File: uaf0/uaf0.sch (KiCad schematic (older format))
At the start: 6 parts, among them X1 Клеммник_х2, X2 Клеммник_х2, X3 Клеммник_х2, X4 Клеммник_х2, X5 Клеммник_х2

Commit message: схема+трассировка, требуется проверка
не установлена ссылка на инстаграм
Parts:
- added C1, C2, C3, C4, C5, C6, C7, C8: Конденсатор_керамический, N_RLC:Конденсатор_SMD_0603, symbol elements:Конденсатор_керамический
- added DD2: 5559ИН10_28(UART-RS485), N_DD:SO-8, symbol elements:5559ИН10_28(UART-RS485)
- added FU1: Предохранитель_0.1A, N_RLC:Предохранитель_SMD_1812, symbol elements:Предохранитель
- added G1: стабилизатор_нерегулируемый_LM1117GS-5.0, N_VD_HL:Транзистор_NPN_SOT223, symbol elements:стабилизатор_нерегулируемый_LM1117GS-5.0
- added G2: стабилизатор_нерегулируемый_XC6206P302MR, N_VD_HL:Транзистор_IRLML6344TR_SOT-23, symbol elements:стабилизатор_нерегулируемый_XC6206P302MR
- added HL1, HL2: Светодиод, N_VD_HL:Светодиод_SMD_0603, symbol elements:Светодиод
- added R1, R10, R11, R2, R3, R4, R5, R6, R7, R8, R9: Резистор_0,065Вт, N_RLC:Резистор_SMD_0603_0,065_Вт, symbol elements:Резистор_0,065Вт
- added VD1: Диод_шоттки_S13, N_VD_HL:Диод_S13_SOD-123, symbol elements:Диод_шоттки
- added X6, X7, X8: Клеммник_х2, N_X:Клеммник_х2_шаг5, symbol elements:Клеммник_х2
- added XP1: Вилка_PLD6_ПРОГ, N_X:Вилка_PLD6_вертикальная, symbol elements:Вилка_PLD6_ПРОГ
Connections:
- net 12V: now also C4.1, G1.3 (6...30_В)
- net GND: now also DD1.21 (GND), DD1.3 (GND), DD1.5 (GND), C1.2, C2.2, C3.1, C4.2, C5.2, C6.2, C7.2, C8.2, DD2.5 (GND), FU1.2, G1.1 (GND), G2.1 (GND), HL1.2, HL2.2, R7.2, X8.1, X8.2, XP1.6 (GND); no longer X2.1, X2.2
- net PD3_INT1: now reaches DD1.1 (PD3(INT1))
- net PB0: now reaches DD1.12 (PB0(ICP1))
- net PB0: now also DD2.2 (nRE), DD2.3 (DE), R7.1
- net PB1_OC1A: now reaches DD1.13 (PB1(OC1A))
- net PB2_OC1B: now reaches DD1.14 (PB2(SS/OC1B))
- net MOSI: now reaches DD1.15 (PB3(MOSI/OC2))
- net MOSI: now also R11.2
- net MISO: now reaches DD1.16 (PB4(MISO))
- net MISO: now also R8.1
- net SCK: now reaches DD1.17 (PB5(SCK))
- net SCK: now also R9.1
- net 5V: now reaches DD1.18 (AVCC)
- net 5V: now also DD1.4 (VCC), DD1.6 (VCC), C1.1, C2.1, C3.2, C5.1, C6.1, DD2.8 (Ucc), G1.2 (5В), G2.3 (3,2...6_В), R1.1, R10.1, R2.1, R4.1, VD1.2
- net 3V: now reaches DD1.20 (AREF)
- net 3V: now also C7.1, C8.1, G2.2 (3В)
- net PC0: now reaches DD1.23 (PCO(ADC0))
- net PC1: now reaches DD1.24 (PC1(ADC1))
- net PC3: now reaches DD1.26 (PC3(ADC3))
- net PC3: now also R5.1
- net SDA: now reaches DD1.27 (PC4(ADC4/SDA))
- net SDA: now also R1.2, X6.1
- net SCL: now reaches DD1.28 (PC5(ADC5/SCL))
- net SCL: now also R2.2, X6.2
- net RES: now reaches DD1.29 (PC6(RESET))
- net RES: now also R10.2, XP1.5 (RST)
- net RX: now reaches DD1.30 (PD0(RXD))
- net RX: now also R3.2
- net TX: now reaches DD1.31 (PD1(TXD))
- net TX: now also R6.2
- net PD2_INT0: now reaches DD1.32 (PD2(INT0))
- new net: DD2.1 (RO), R3.1
- new net: DD2.4 (DI), R6.1
- new net: R8.2, XP1.1 (MISO)
- new net: R9.2, XP1.3 (SCK)
- new net: R11.1, XP1.4 (MOSI)
- new net: HL2.1, R5.2
- new net: HL1.1, R4.2
- new net PWR_GND: FU1.1, X2.1, X2.2
- new net RS485_A: DD2.6 (AY), X7.1
- new net RS485_B: DD2.7 (BZ), X7.2
- new net VCC_PROG: VD1.1, XP1.2 (VCC)
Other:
- moved on the sheet: DD1, X1, X2, X3, X4, X5

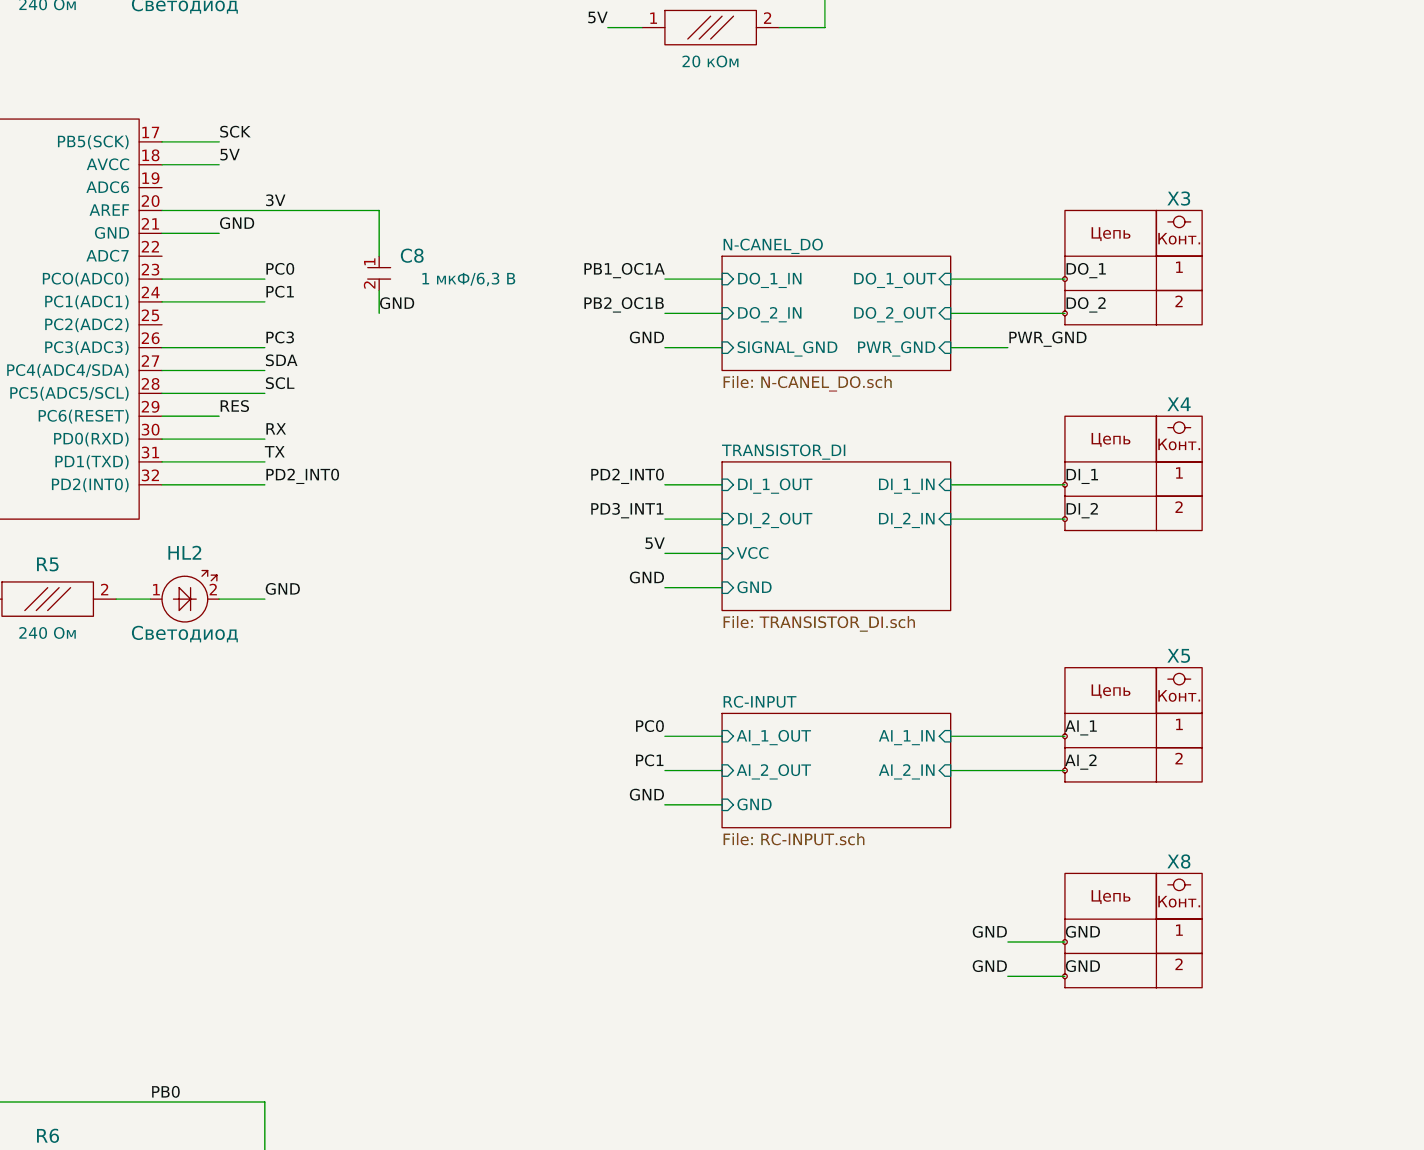
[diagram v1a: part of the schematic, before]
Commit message: исправлена шелкография, добавлены файлы производства v0
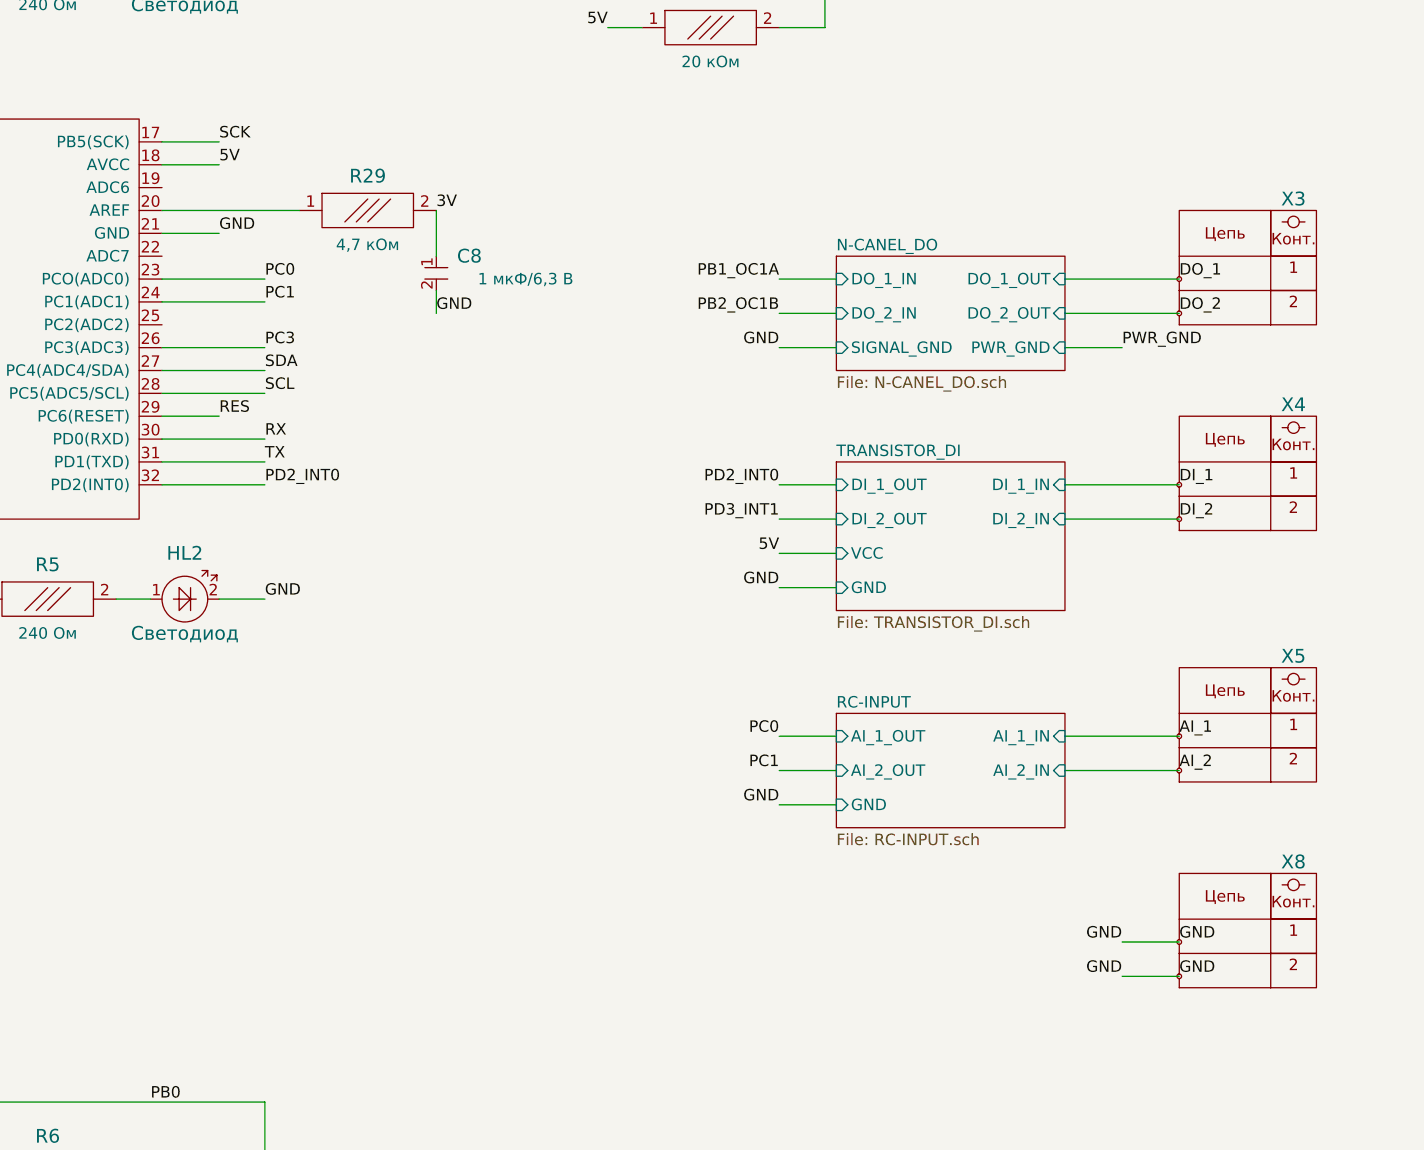
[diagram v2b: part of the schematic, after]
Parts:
- added R29: Резистор_0,065Вт, N_RLC:Резистор_SMD_0603_0,065_Вт, symbol elements:Резистор_0,065Вт
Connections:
- net 3V: now also R29.2; no longer DD1.20 (AREF)
- new net: DD1.20 (AREF), R29.1
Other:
- moved on the sheet: C8, X3, X4, X5, X8
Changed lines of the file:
@@
 L elements:Клеммник_х2 X3
 U 1 1 5DAC06C7
-P 9500 3100
-F 0 "X3" H 9000 3450 60  0000 C CNN
-F 1 "Клеммник_х2" H 9450 2725 60  0001 C CNN
-F 2 "N_X:Клеммник_х2_шаг5" H 9500 3100 60  0001 C CNN
-F 3 "" H 9500 3100 60  0001 C CNN
-	1    9500 3100
+P 10000 3100
+F 0 "X3" H 9500 3450 60  0000 C CNN
+F 1 "Клеммник_х2" H 9950 2725 60  0001 C CNN
+F 2 "N_X:Клеммник_х2_шаг5" H 10000 3100 60  0001 C CNN
+F 3 "" H 10000 3100 60  0001 C CNN
+	1    10000 3100
 	-1   0    0    -1
 $EndComp
-Text Label 9500 3100 0    50   ~ 0
+Text Label 10000 3100 0    50   ~ 0
 DO_1
-Text Label 9500 3250 0    50   ~ 0
+Text Label 10000 3250 0    50   ~ 0
 DO_2
 $Comp
 L elements:Клеммник_х2 X4
 U 1 1 5DAC910B
-P 9500 4000
-F 0 "X4" H 9000 4350 60  0000 C CNN
-F 1 "Клеммник_х2" H 9450 3625 60  0001 C CNN
-F 2 "N_X:Клеммник_х2_шаг5" H 9500 4000 60  0001 C CNN
-F 3 "" H 9500 4000 60  0001 C CNN
-	1    9500 4000
+P 10000 4000
+F 0 "X4" H 9500 4350 60  0000 C CNN
+F 1 "Клеммник_х2" H 9950 3625 60  0001 C CNN
+F 2 "N_X:Клеммник_х2_шаг5" H 10000 4000 60  0001 C CNN
+F 3 "" H 10000 4000 60  0001 C CNN
+	1    10000 4000
 	-1   0    0    -1
 $EndComp
-Text Label 9500 4000 0    50   ~ 0
+Text Label 10000 4000 0    50   ~ 0
 DI_1
-Text Label 9500 4150 0    50   ~ 0
+Text Label 10000 4150 0    50   ~ 0
 DI_2
 $Comp
 L elements:Клеммник_х2 X5
 U 1 1 5DACA5D7
-P 9500 5100
-F 0 "X5" H 9000 5450 60  0000 C CNN
-F 1 "Клеммник_х2" H 9450 4725 60  0001 C CNN
-F 2 "N_X:Клеммник_х2_шаг5" H 9500 5100 60  0001 C CNN
-F 3 "" H 9500 5100 60  0001 C CNN
-	1    9500 5100
+P 10000 5100
+F 0 "X5" H 9500 5450 60  0000 C CNN
+F 1 "Клеммник_х2" H 9950 4725 60  0001 C CNN
+F 2 "N_X:Клеммник_х2_шаг5" H 10000 5100 60  0001 C CNN
+F 3 "" H 10000 5100 60  0001 C CNN
+	1    10000 5100
 	-1   0    0    -1
 $EndComp
-Text Label 9500 5100 0    50   ~ 0
+Text Label 10000 5100 0    50   ~ 0
 AI_1
-Text Label 9500 5250 0    50   ~ 0
+Text Label 10000 5250 0    50   ~ 0
 AI_2
 $Comp
@@
 Text Label 5250 1500 0    50   ~ 0
 GND
-Text Label 6000 2800 0    50   ~ 0
+Text Label 6750 2800 0    50   ~ 0
 3V
 Text Label 5800 2600 0    50   ~ 0
@@
 Text Label 3250 3000 2    50   ~ 0
 5V
-Wire Wire Line
-	5550 2800 6500 2800
 $Comp
 L elements:Конденсатор_керамический C8
 U 1 1 5DAE7890
-P 6500 3050
-F 0 "C8" V 6450 3250 60  0000 R CNN
-F 1 "Конденсатор_керамический" H 6600 2950 60  0001 C CNN
-F 2 "N_RLC:Конденсатор_SMD_0603" H 6500 3050 60  0001 C CNN
-F 3 "" H 6500 3050 60  0001 C CNN
-F 4 "1 мкФ/6,3 В" V 6550 3650 50  0000 R CNN "Номинал"
-F 5 "С111" H 6500 3050 50  0001 C CNN "УГО"
-	1    6500 3050
+P 6750 3050
+F 0 "C8" V 6700 3250 60  0000 R CNN
+F 1 "Конденсатор_керамический" H 6850 2950 60  0001 C CNN
+F 2 "N_RLC:Конденсатор_SMD_0603" H 6750 3050 60  0001 C CNN
+F 3 "" H 6750 3050 60  0001 C CNN
+F 4 "1 мкФ/6,3 В" V 6800 3650 50  0000 R CNN "Номинал"
+F 5 "С111" H 6750 3050 50  0001 C CNN "УГО"
+	1    6750 3050
 	0    1    1    0
 $EndComp
 Wire Wire Line
-	6500 2800 6500 3000
-Wire Wire Line
-	6500 3150 6500 3250
-Text Label 6500 3250 0    50   ~ 0
+	6750 2800 6750 3000
+Wire Wire Line
+	6750 3150 6750 3250
+Text Label 6750 3250 0    50   ~ 0
 GND
 $Comp
@@
 	1000 3000 1750 3000
 $Sheet
-S 8000 3900 1000 650
+S 8500 3900 1000 650
 U 5DB51AF8
 F0 "TRANSISTOR_DI" 50
 F1 "TRANSISTOR_DI.sch" 50
-F2 "DI_1_IN" I R 9000 4000 50
-F3 "GND" I L 8000 4450 50
-F4 "DI_2_IN" I R 9000 4150 50
-F5 "DI_2_OUT" I L 8000 4150 50
-F6 "DI_1_OUT" I L 8000 4000 50
-F7 "VCC" I L 8000 4300 50
+F2 "DI_1_IN" I R 9500 4000 50
+F3 "GND" I L 8500 4450 50
+F4 "DI_2_IN" I R 9500 4150 50
+F5 "DI_2_OUT" I L 8500 4150 50
+F6 "DI_1_OUT" I L 8500 4000 50
+F7 "VCC" I L 8500 4300 50
 $EndSheet
 Wire Wire Line
-	9000 4000 9500 4000
-Wire Wire Line
-	9000 4150 9500 4150
-Wire Wire Line
-	8000 4450 7750 4450
-Text Label 7750 4450 2    50   ~ 0
-GND
-Wire Wire Line
-	8000 4300 7750 4300
-Text Label 7750 4300 2    50   ~ 0
-5V
-Wire Wire Line
-	8000 4150 7750 4150
-Wire Wire Line
-	8000 4000 7750 4000
+	9500 4000 10000 4000
+Wire Wire Line
+	9500 4150 10000 4150
+Wire Wire Line
+	8500 4450 8250 4450
+Text Label 8250 4450 2    50   ~ 0
+GND
+Wire Wire Line
+	8500 4300 8250 4300
+Text Label 8250 4300 2    50   ~ 0
+5V
+Wire Wire Line
+	8500 4150 8250 4150
+Wire Wire Line
+	8500 4000 8250 4000
 Text Label 6000 3900 0    50   ~ 0
 TX
@@
 Text Label 6000 4000 0    50   ~ 0
 PD2_INT0
-Text Label 7750 4000 2    50   ~ 0
+Text Label 8250 4000 2    50   ~ 0
 PD2_INT0
 Text Label 3000 2500 2    50   ~ 0
@@
 Wire Wire Line
 	3000 2500 3500 2500
-Text Label 7750 4150 2    50   ~ 0
+Text Label 8250 4150 2    50   ~ 0
 PD3_INT1
 Text Label 3000 3700 2    50   ~ 0
@@
 Wire Wire Line
 	3000 3800 3500 3800
-Text Label 7750 3100 2    50   ~ 0
+Text Label 8250 3100 2    50   ~ 0
 PB1_OC1A
-Text Label 7750 3250 2    50   ~ 0
+Text Label 8250 3250 2    50   ~ 0
 PB2_OC1B
 Text Label 6000 3600 0    50   ~ 0
@@
 	3500 3000 3250 3000
 $Sheet
-S 8000 5000 1000 500
+S 8500 5000 1000 500
 U 5DBE4A0C
 F0 "RC-INPUT" 50
 F1 "RC-INPUT.sch" 50
-F2 "AI_1_OUT" I L 8000 5100 50
-F3 "AI_1_IN" I R 9000 5100 50
-F4 "AI_2_OUT" I L 8000 5250 50
-F5 "AI_2_IN" I R 9000 5250 50
-F6 "GND" I L 8000 5400 50
+F2 "AI_1_OUT" I L 8500 5100 50
+F3 "AI_1_IN" I R 9500 5100 50
+F4 "AI_2_OUT" I L 8500 5250 50
+F5 "AI_2_IN" I R 9500 5250 50
+F6 "GND" I L 8500 5400 50
 $EndSheet
 Wire Wire Line
-	8000 5400 7750 5400
-Text Label 7750 5400 2    50   ~ 0
-GND
-Wire Wire Line
-	9000 5100 9500 5100
-Wire Wire Line
-	9000 5250 9500 5250
+	8500 5400 8250 5400
+Text Label 8250 5400 2    50   ~ 0
+GND
+Wire Wire Line
+	9500 5100 10000 5100
+Wire Wire Line
+	9500 5250 10000 5250
 Text Label 6000 3200 0    50   ~ 0
 PC1
@@
 Wire Wire Line
 	5550 3200 6000 3200
-Text Label 7750 5250 2    50   ~ 0
+Text Label 8250 5250 2    50   ~ 0
 PC1
-Text Label 7750 5100 2    50   ~ 0
+Text Label 8250 5100 2    50   ~ 0
 PC0
 Wire Wire Line
-	8000 5250 7750 5250
-Wire Wire Line
-	8000 5100 7750 5100
+	8500 5250 8250 5250
+Wire Wire Line
+	8500 5100 8250 5100
 $Comp
 L elements:Клеммник_х2 X6
@@
 Connection ~ 1750 1750
 $Sheet
-S 8000 3000 1000 500
+S 8500 3000 1000 500
 U 5DC52DBF
 F0 "N-CANEL_DO" 50
 F1 "N-CANEL_DO.sch" 50
-F2 "DO_1_OUT" I R 9000 3100 50
-F3 "DO_1_IN" I L 8000 3100 50
-F4 "SIGNAL_GND" I L 8000 3400 50
-F5 "PWR_GND" I R 9000 3400 50
-F6 "DO_2_OUT" I R 9000 3250 50
-F7 "DO_2_IN" I L 8000 3250 50
+F2 "DO_1_OUT" I R 9500 3100 50
+F3 "DO_1_IN" I L 8500 3100 50
+F4 "SIGNAL_GND" I L 8500 3400 50
+F5 "PWR_GND" I R 9500 3400 50
+F6 "DO_2_OUT" I R 9500 3250 50
+F7 "DO_2_IN" I L 8500 3250 50
 $EndSheet
 Wire Wire Line
-	9000 3100 9500 3100
-Wire Wire Line
-	9000 3250 9500 3250
-Wire Wire Line
-	9000 3400 9250 3400
-Text Label 9250 3400 0    50   ~ 0
+	9500 3100 10000 3100
+Wire Wire Line
+	9500 3250 10000 3250
+Wire Wire Line
+	9500 3400 9750 3400
+Text Label 9750 3400 0    50   ~ 0
 PWR_GND
 Wire Wire Line
-	8000 3250 7750 3250
-Wire Wire Line
-	8000 3100 7750 3100
-Wire Wire Line
-	8000 3400 7750 3400
-Text Label 7750 3400 2    50   ~ 0
+	8500 3250 8250 3250
+Wire Wire Line
+	8500 3100 8250 3100
+Wire Wire Line
+	8500 3400 8250 3400
+Text Label 8250 3400 2    50   ~ 0
 GND
 $Comp
@@
 L elements:Клеммник_х2 X8
 U 1 1 5DD0A190
-P 9500 6000
-F 0 "X8" H 9000 6350 60  0000 C CNN
-F 1 "Клеммник_х2" H 9450 5625 60  0001 C CNN
-F 2 "N_X:Клеммник_х2_шаг5" H 9500 6000 60  0001 C CNN
-F 3 "" H 9500 6000 60  0001 C CNN
-	1    9500 6000
+P 10000 6000
+F 0 "X8" H 9500 6350 60  0000 C CNN
+F 1 "Клеммник_х2" H 9950 5625 60  0001 C CNN
+F 2 "N_X:Клеммник_х2_шаг5" H 10000 6000 60  0001 C CNN
+F 3 "" H 10000 6000 60  0001 C CNN
+	1    10000 6000
 	-1   0    0    -1
 $EndComp
-Text Label 9500 6000 0    50   ~ 0
-GND
-Text Label 9500 6150 0    50   ~ 0
-GND
-Wire Wire Line
-	9500 6000 9250 6000
-Text Label 9250 6000 2    50   ~ 0
-GND
-Wire Wire Line
-	9500 6150 9250 6150
-Text Label 9250 6150 2    50   ~ 0
+Text Label 10000 6000 0    50   ~ 0
+GND
+Text Label 10000 6150 0    50   ~ 0
+GND
+Wire Wire Line
+	10000 6000 9750 6000
+Text Label 9750 6000 2    50   ~ 0
+GND
+Wire Wire Line
+	10000 6150 9750 6150
+Text Label 9750 6150 2    50   ~ 0
 GND
 Text Label 1500 5400 2    50   ~ 0
@@
 Text Label 4500 4500 2    50   ~ 0
 PC3
+$Comp
+L elements:Резистор_0,065Вт R29
+U 1 1 5DADFAA1
+P 6450 2800
+F 0 "R29" H 6450 2950 60  0000 C CNN
+F 1 "Резистор_0,065Вт" H 6450 2650 60  0001 C CNN
+F 2 "N_RLC:Резистор_SMD_0603_0,065_Вт" H 6450 2800 60  0001 C CNN
+F 3 "" H 6450 2800 60  0001 C CNN
+F 4 "R101" H 6450 2800 50  0001 C CNN "УГО"
+F 5 "4,7 кОм" H 6450 2650 50  0000 C CNN "Номинал"
+	1    6450 2800
+	1    0    0    -1
+$EndComp
+Wire Wire Line
+	6150 2800 5550 2800
 $EndSCHEMATC

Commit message: скетч для генератора "колоколов"
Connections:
- net DI_1: now also X4.2; no longer X4.1
- net DI_2: now also X4.1; no longer X4.2
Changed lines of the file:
@@
 $EndComp
 Text Label 10000 4000 0    50   ~ 0
+DI_2
+Text Label 10000 4150 0    50   ~ 0
 DI_1
-Text Label 10000 4150 0    50   ~ 0
-DI_2
 $Comp
 L elements:Клеммник_х2 X5
@@
 F7 "VCC" I L 8500 4300 50
 $EndSheet
-Wire Wire Line
-	9500 4000 10000 4000
-Wire Wire Line
-	9500 4150 10000 4150
 Wire Wire Line
 	8500 4450 8250 4450
@@
 Wire Wire Line
 	6150 2800 5550 2800
+Wire Wire Line
+	9500 4000 10000 4000
+Wire Wire Line
+	9500 4150 10000 4150
 $EndSCHEMATC
